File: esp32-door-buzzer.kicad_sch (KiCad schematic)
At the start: 13 parts, among them J1 ESP32-S3, J2 ESP32-S3, J3 Conn_01x06_Pin, J4 Conn_01x02_Pin, K1 HK4100F-DC5V-SHG, Q1 NPN, U1 Optocoupler_DC_PhotoNPN_AKEC, U2 L78L12_TO92

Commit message: Change transistor to a mosfet
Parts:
- Q1: value NPN -> NMOS; symbol Simulation_SPICE:NPN -> Simulation_SPICE:NMOS
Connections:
- net GND: now also Q1.3 (S); no longer Q1.1 (E)
- net at D2.2 (A), K1.9: now also Q1.1 (D); no longer Q1.3 (C)
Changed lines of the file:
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@@
 	)
 	(symbol
-		(lib_id "Simulation_SPICE:NPN")
+		(lib_id "Simulation_SPICE:NMOS")
 		(at 91.44 83.82 0)
 		(unit 1)
@@
 		(fields_autoplaced yes)
 		(property "Reference" "Q1"
-			(at 96.52 82.5499 0)
+			(at 97.79 82.5499 0)
 			(effects
 				(font
@@
 			)
 		)
-		(property "Value" "NPN"
-			(at 96.52 85.0899 0)
+		(property "Value" "NMOS"
+			(at 97.79 85.0899 0)
 			(effects
 				(font
@@
 		)
 		(property "Footprint" "Package_TO_SOT_THT:TO-92_Inline_Wide"
-			(at 154.94 83.82 0)
+			(at 96.52 81.28 0)
 			(effects
 				(font
@@
 			)
 		)
-		(property "Datasheet" "https://ngspice.sourceforge.io/docs/ngspice-html-manual/manual.xhtml#cha_BJTs"
-			(at 154.94 83.82 0)
+		(property "Datasheet" "https://ngspice.sourceforge.io/docs/ngspice-html-manual/manual.xhtml#cha_MOSFETs"
+			(at 91.44 96.52 0)
 			(effects
 				(font
@@
 			)
 		)
-		(property "Description" "Bipolar transistor symbol for simulation only, substrate tied to the emitter"
+		(property "Description" "N-MOSFET transistor, drain/source/gate"
 			(at 91.44 83.82 0)
 			(effects
@@
 			)
 		)
-		(property "Sim.Device" "NPN"
-			(at 91.44 83.82 0)
+		(property "Sim.Device" "NMOS"
+			(at 91.44 100.965 0)
 			(effects
 				(font
@@
 			)
 		)
-		(property "Sim.Type" "GUMMELPOON"
-			(at 91.44 83.82 0)
+		(property "Sim.Type" "VDMOS"
+			(at 91.44 102.87 0)
 			(effects
 				(font
@@
 			)
 		)
-		(property "Sim.Pins" "1=C 2=B 3=E"
-			(at 91.44 83.82 0)
+		(property "Sim.Pins" "1=D 2=G 3=S"
+			(at 91.44 99.06 0)
 			(effects
 				(font

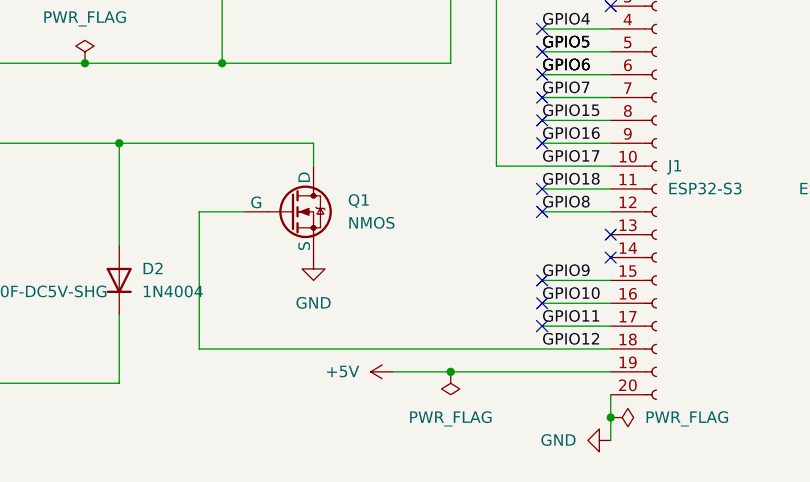
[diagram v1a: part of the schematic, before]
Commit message: Add resistors to manage the mosfet properly
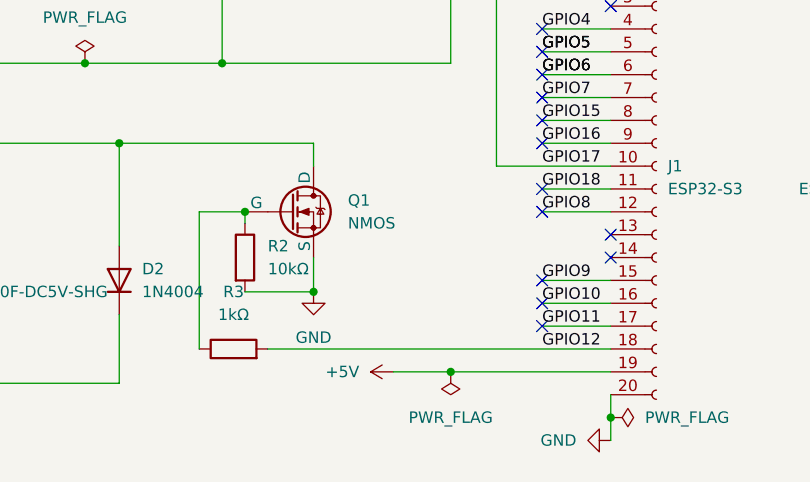
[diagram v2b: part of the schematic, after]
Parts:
- added R2: 10kΩ, symbol Device:R
- added R3: 1kΩ, symbol Device:R
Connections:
- net GND: now also R2.2
- net GPIO12: now also R3.2; no longer Q1.2 (G)
- new net: Q1.2 (G), R2.1, R3.1
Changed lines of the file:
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@@
+	)
+	(junction
+		(at 86.36 83.82)
+		(diameter 0)
+		(color 0 0 0 0)
 	)
 	(junction
@@
 		(color 0 0 0 0)
 	)
+	(junction
+		(at 93.98 92.71)
+		(diameter 0)
+		(color 0 0 0 0)
+	)
 	(no_connect
 		(at 119.38 68.58)
@@
 	(wire
 		(pts
+			(xy 86.36 83.82) (xy 86.36 85.09)
+		)
+		(stroke
+			(width 0)
+			(type default)
+		)
+	)
+	(wire
+		(pts
 			(xy 16.51 22.86) (xy 26.67 22.86)
 		)
@@
 	(wire
 		(pts
+			(xy 86.36 92.71) (xy 93.98 92.71)
+		)
+		(stroke
+			(width 0)
+			(type default)
+		)
+	)
+	(wire
+		(pts
 			(xy 81.28 83.82) (xy 81.28 99.06)
 		)
@@
 	(wire
 		(pts
-			(xy 81.28 99.06) (xy 127 99.06)
-		)
-		(stroke
-			(width 0)
-			(type default)
-		)
-	)
-	(wire
-		(pts
 			(xy 34.29 107.95) (xy 26.67 107.95)
 		)
@@
 	(wire
 		(pts
+			(xy 88.9 99.06) (xy 127 99.06)
+		)
+		(stroke
+			(width 0)
+			(type default)
+		)
+	)
+	(wire
+		(pts
 			(xy 119.38 83.82) (xy 127 83.82)
 		)
@@
 		(pts
 			(xy 21.59 15.24) (xy 21.59 34.29)
+		)
+		(stroke
+			(width 0)
+			(type default)
+		)
+	)
+	(wire
+		(pts
+			(xy 93.98 92.71) (xy 93.98 88.9)
 		)
 		(stroke
@@
 	)
 	(symbol
+		(lib_id "Device:R")
+		(at 86.36 88.9 0)
+		(unit 1)
+		(exclude_from_sim no)
+		(in_bom yes)
+		(on_board yes)
+		(dnp no)
+		(fields_autoplaced yes)
+		(property "Reference" "R2"
+			(at 88.9 87.6299 0)
+			(effects
+				(font
+					(size 1.27 1.27)
+				)
+				(justify left)
+			)
+		)
+		(property "Value" "10kΩ"
+			(at 88.9 90.1699 0)
+			(effects
+				(font
+					(size 1.27 1.27)
+				)
+				(justify left)
+			)
+		)
+		(property "Footprint" ""
+			(at 84.582 88.9 90)
+			(effects
+				(font
+					(size 1.27 1.27)
+				)
+				(hide yes)
+			)
+		)
+		(property "Datasheet" "~"
+			(at 86.36 88.9 0)
+			(effects
+				(font
+					(size 1.27 1.27)
+				)
+				(hide yes)
+			)
+		)
+		(property "Description" "Resistor"
+			(at 86.36 88.9 0)
+			(effects
+				(font
+					(size 1.27 1.27)
+				)
+				(hide yes)
+			)
+		)
+		(pin "1"
+		)
+		(pin "2"
+		)
+		(instances
+			(project ""
+				(path "/d95df0c9-82cd-44b1-ab7a-56e5f7ebbfca"
+					(reference "R2")
+					(unit 1)
+				)
+			)
+		)
+	)
+	(symbol
 		(lib_id "power:GND")
 		(at 162.56 101.6 90)
@@
 	(symbol
 		(lib_id "power:GND")
-		(at 93.98 88.9 0)
+		(at 93.98 92.71 0)
 		(unit 1)
 		(exclude_from_sim no)
@@
 		(fields_autoplaced yes)
 		(property "Reference" "#PWR010"
-			(at 93.98 95.25 0)
+			(at 93.98 99.06 0)
 			(effects
 				(font
@@
 		)
 		(property "Value" "GND"
-			(at 93.98 93.98 0)
+			(at 93.98 97.79 0)
 			(effects
 				(font
@@
 		)
 		(property "Footprint" ""
-			(at 93.98 88.9 0)
+			(at 93.98 92.71 0)
 			(effects
 				(font
@@
 		)
 		(property "Datasheet" ""
-			(at 93.98 88.9 0)
+			(at 93.98 92.71 0)
 			(effects
 				(font
@@
 		)
 		(property "Description" "Power symbol creates a global label with name \"GND\" , ground"
-			(at 93.98 88.9 0)
+			(at 93.98 92.71 0)
 			(effects
 				(font
@@
 					(unit 1)
 				)
+			)
+		)
+	)
+	(symbol
+		(lib_id "Device:R")
+		(at 85.09 99.06 90)
+		(unit 1)
+		(exclude_from_sim no)
+		(in_bom yes)
+		(on_board yes)
+		(dnp no)
+		(fields_autoplaced yes)
+		(property "Reference" "R3"
+			(at 85.09 92.71 90)
+			(effects
+				(font
+					(size 1.27 1.27)
+				)
+			)
+		)
+		(property "Value" "1kΩ"
+			(at 85.09 95.25 90)
+			(effects
+				(font
+					(size 1.27 1.27)
+				)
+			)
+		)
+		(property "Footprint" ""
+			(at 85.09 100.838 90)
+			(effects
+				(font
+					(size 1.27 1.27)
+				)
+				(hide yes)
+			)
+		)
+		(property "Datasheet" "~"
+			(at 85.09 99.06 0)
+			(effects
+				(font
+					(size 1.27 1.27)
+				)
+				(hide yes)
+			)
+		)
+		(property "Description" "Resistor"
+			(at 85.09 99.06 0)
+			(effects
+				(font
+					(size 1.27 1.27)
+				)
+				(hide yes)
+			)
+		)
+		(pin "1"
+		)
+		(pin "2"
+		)
+		(instances
+			(project ""
+				(path "/d95df0c9-82cd-44b1-ab7a-56e5f7ebbfca"
+					(reference "R3")
+					(unit 1)
+				)
